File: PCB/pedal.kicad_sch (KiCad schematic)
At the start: 5 parts, among them J1 Jack-DC, J2 Barrel_Jack, J3 Barrel_Jack, J4 Barrel_Jack

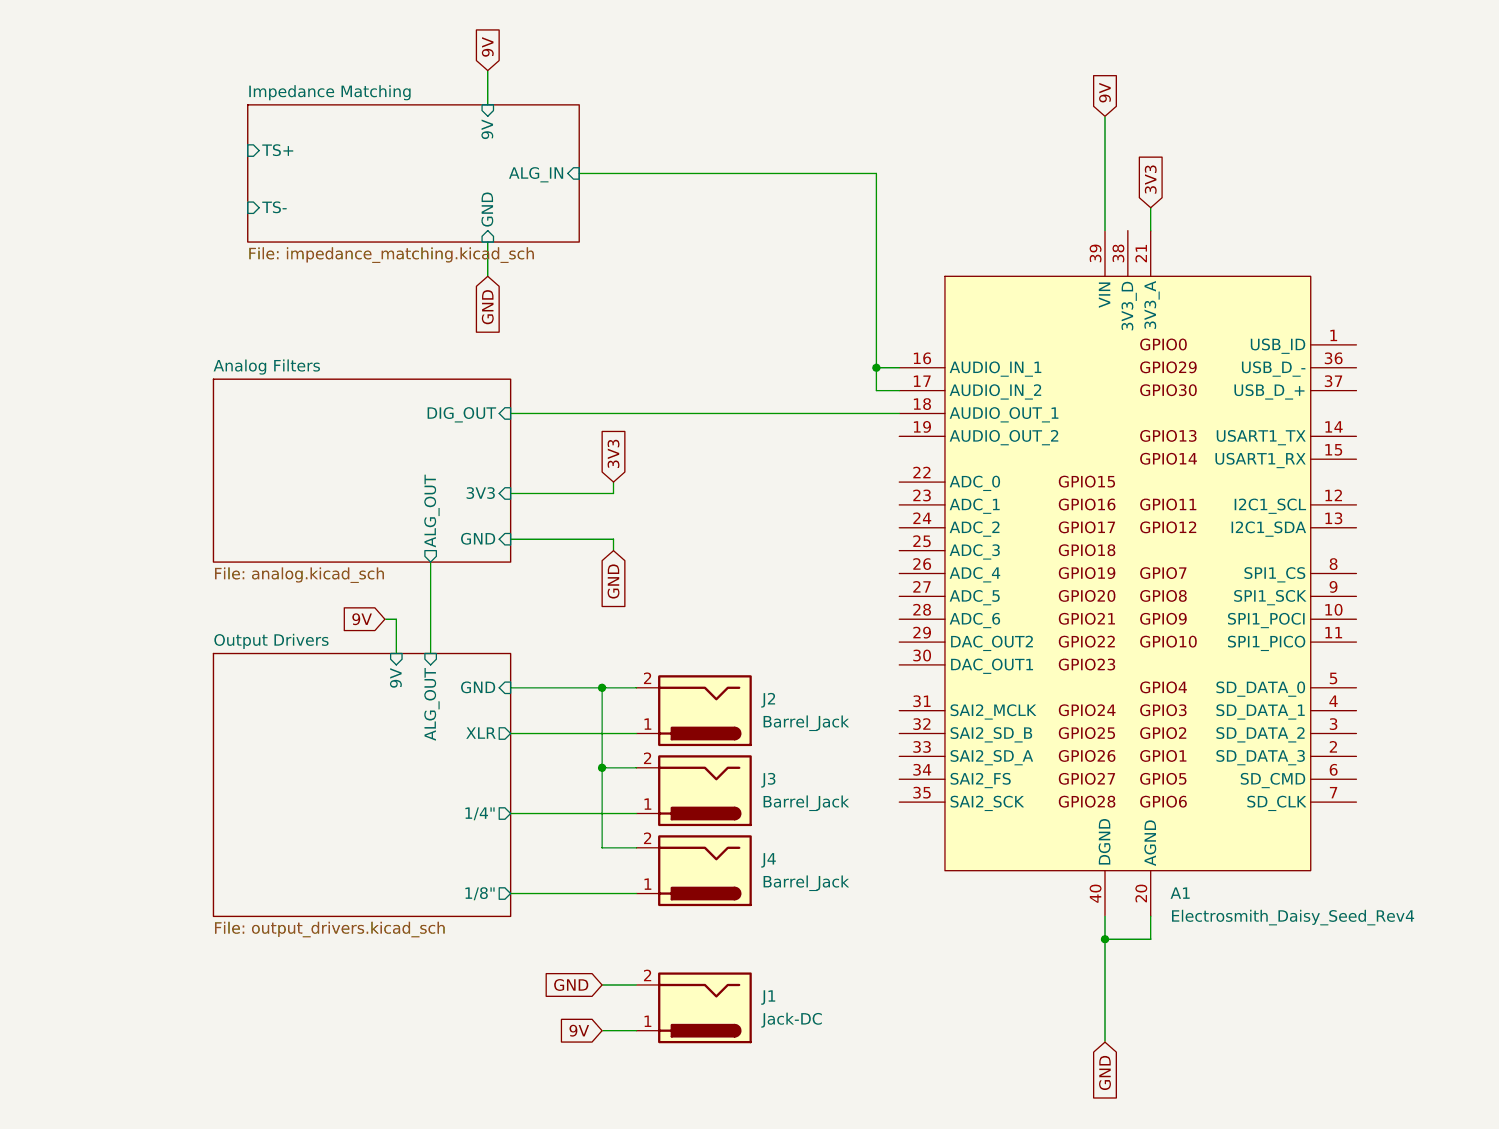
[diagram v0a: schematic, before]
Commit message: reorganized MATLAB and PCB files, merged analog design into main KiCAD schematic, added MATLAB noise analysis
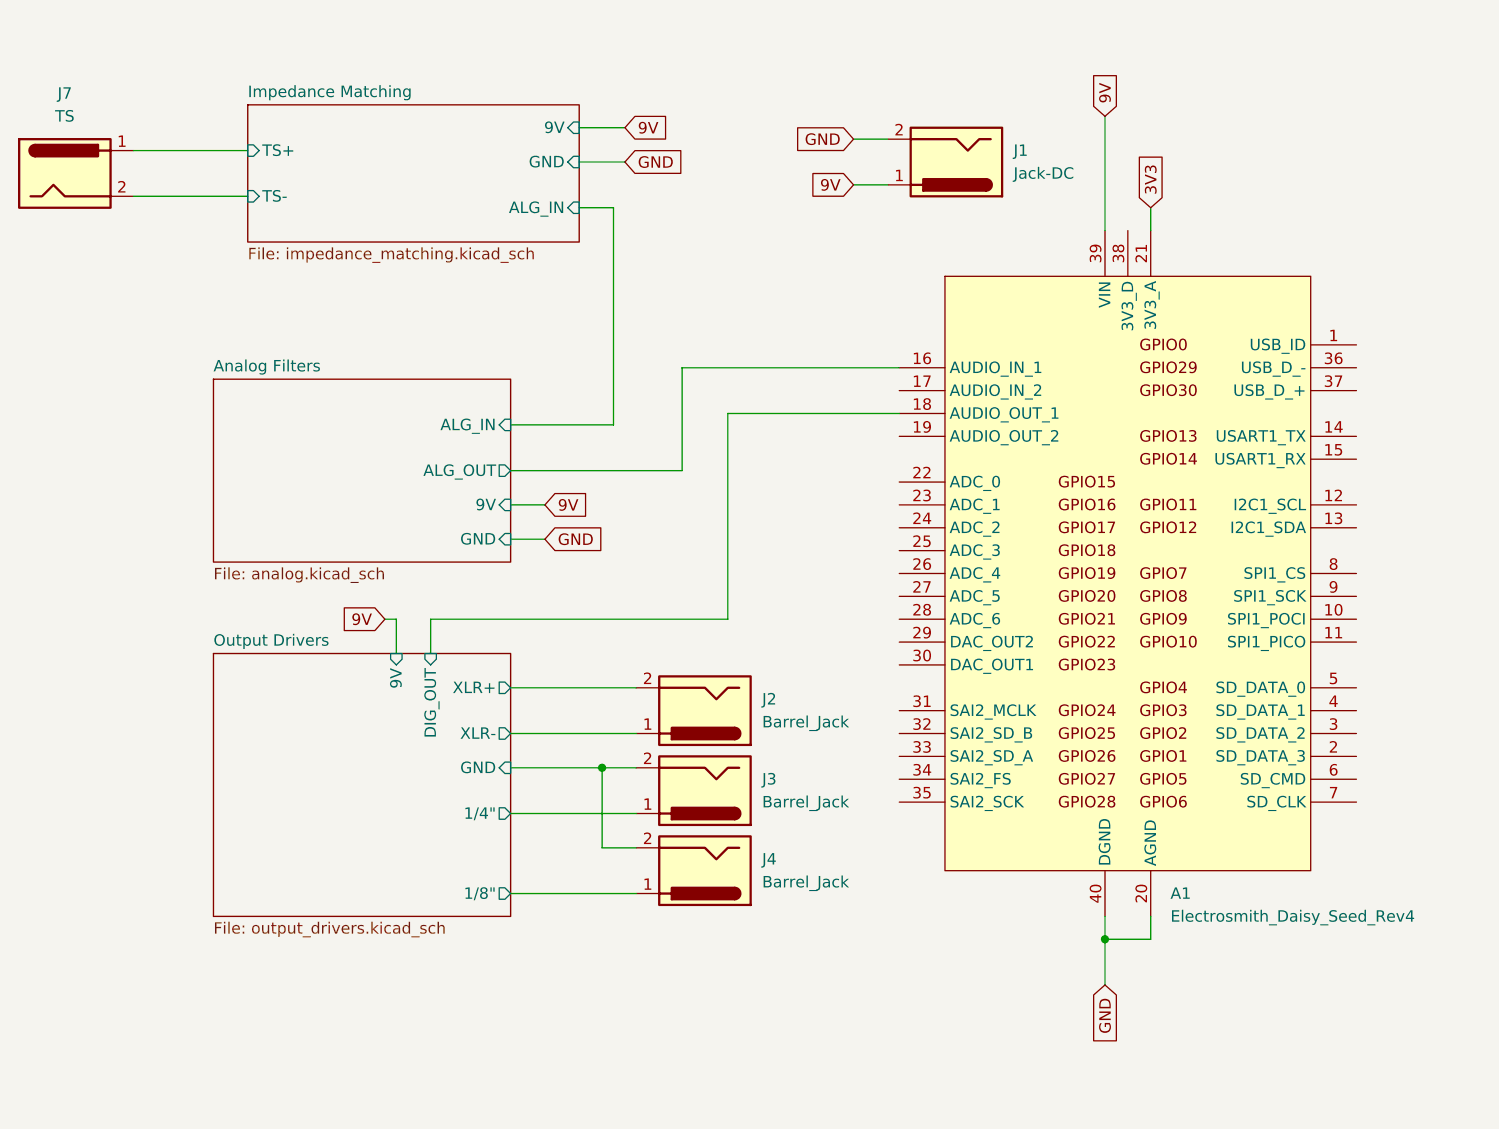
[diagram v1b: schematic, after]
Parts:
- added J7: TS, symbol Connector:Jack-DC
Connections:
- net Analog Filters/ALG_OUT: now also A1.16 (AUDIO_IN_1)
- net Impedance Matching/TS+: now also J7.1
- net Impedance Matching/TS-: now also J7.2
- net Output Drivers/GND: no longer J2.2
- net Analog Filters/DIG_OUT renamed Output Drivers/DIG_OUT
- net Impedance Matching/ALG_IN: no longer names the net of A1.17 (AUDIO_IN_2)
- net Impedance Matching/ALG_IN: no longer A1.16 (AUDIO_IN_1)
- net Output Drivers/XLR renamed Output Drivers/XLR-
- new net Output Drivers/XLR+: J2.2
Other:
- sheet Analog Filters ports: added 9V, ALG_IN; removed 3V3, DIG_OUT
- sheet Output Drivers ports: added DIG_OUT, XLR+, XLR-; removed ALG_OUT, XLR
- moved on the sheet: J1
